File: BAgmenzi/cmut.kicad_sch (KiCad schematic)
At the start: 14 parts, among them J4 connector for CMUT

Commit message: added libraries, other changes in sch, started pcb
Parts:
- renumbered C60 to C61, C61 to C62, C62 to C63, R45 to R41, R44 to R43, R43 to R44
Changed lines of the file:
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@@
 		(dnp no)
 		(fields_autoplaced yes)
-		(property "Reference" "R45"
+		(property "Reference" "R41"
 			(at 134.62 41.9099 0)
 			(effects
@@
 			(project "BAgmenzi"
 				(path "/8cc4acae-3f14-463c-b0a0-3bc1c8d05954/edb8e8bc-fb53-4a31-8600-d64a48325b03"
-					(reference "R45")
+					(reference "R41")
 					(unit 1)
 				)
@@
 		(dnp no)
 		(fields_autoplaced yes)
-		(property "Reference" "C62"
+		(property "Reference" "C63"
 			(at 142.24 130.8099 0)
 			(effects
@@
 			(project ""
 				(path "/8cc4acae-3f14-463c-b0a0-3bc1c8d05954/edb8e8bc-fb53-4a31-8600-d64a48325b03"
-					(reference "C62")
+					(reference "C63")
 					(unit 1)
 				)
@@
 		(on_board yes)
 		(dnp no)
-		(property "Reference" "C61"
+		(property "Reference" "C62"
 			(at 118.11 130.302 0)
 			(effects
@@
 			(project "BAgmenzi"
 				(path "/8cc4acae-3f14-463c-b0a0-3bc1c8d05954/edb8e8bc-fb53-4a31-8600-d64a48325b03"
-					(reference "C61")
+					(reference "C62")
 					(unit 1)
 				)
@@
 		(dnp no)
 		(fields_autoplaced yes)
-		(property "Reference" "R44"
+		(property "Reference" "R43"
 			(at 127 69.8499 0)
 			(effects
@@
 			(project "BAgmenzi"
 				(path "/8cc4acae-3f14-463c-b0a0-3bc1c8d05954/edb8e8bc-fb53-4a31-8600-d64a48325b03"
-					(reference "R44")
+					(reference "R43")
 					(unit 1)
 				)
@@
 		(on_board yes)
 		(dnp no)
-		(property "Reference" "C60"
+		(property "Reference" "C61"
 			(at 134.112 61.722 90)
 			(effects
@@
 			(project "BAgmenzi"
 				(path "/8cc4acae-3f14-463c-b0a0-3bc1c8d05954/edb8e8bc-fb53-4a31-8600-d64a48325b03"
-					(reference "C60")
+					(reference "C61")
 					(unit 1)
 				)
@@
 		(dnp no)
 		(fields_autoplaced yes)
-		(property "Reference" "R43"
+		(property "Reference" "R44"
 			(at 123.19 113.03 90)
 			(effects
@@
 			(project "BAgmenzi"
 				(path "/8cc4acae-3f14-463c-b0a0-3bc1c8d05954/edb8e8bc-fb53-4a31-8600-d64a48325b03"
-					(reference "R43")
-					(unit 1)
-				)
+					(reference "R44")
+					(unit 1)
+				)

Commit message: changed VRX rail and deleted U12
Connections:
- net PULSE_HV_IN renamed PULSE_HV
- net RX_OUT renamed RX_IN
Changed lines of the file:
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@@
 		)
 	)
-	(hierarchical_label "PULSE_HV_IN"
+	(global_label "PULSE_HV"
 		(shape input)
 		(at 68.58 87.63 180)
+		(fields_autoplaced yes)
 		(effects
 			(font
@@
 			(justify right)
 		)
+		(property "Intersheetrefs" "${INTERSHEET_REFS}"
+			(at 56.221 87.63 0)
+			(effects
+				(font
+					(size 1.27 1.27)
+				)
+				(justify right)
+			)
+		)
 	)
-	(hierarchical_label "RX_OUT"
+	(global_label "RX_IN"
 		(shape output)
 		(at 67.31 93.98 180)
+		(fields_autoplaced yes)
 		(effects
 			(font
@@
 			(justify right)
 		)
+		(property "Intersheetrefs" "${INTERSHEET_REFS}"
+			(at 58.9424 93.98 0)
+			(effects
+				(font
+					(size 1.27 1.27)
+				)
+				(justify right)
+			)
+		)
 	)

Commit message: started layout, front v backside
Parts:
- C61, C62, C63, R43, R44: footprint (none) -> EEG_PcbLib:0402
- J4: footprint (none) -> cmut_dummy:cmut-dummy
- JP1, JP2, JP3, JP4, JP5: footprint (none) -> Jumper:SolderJumper-3_P1.3mm_Open_Pad1.0x1.5mm
- R41, R42: footprint (none) -> Resistor_SMD:R_0402_1005Metric
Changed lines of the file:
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@@
 			)
 		)
-		(property "Footprint" ""
+		(property "Footprint" "Resistor_SMD:R_0402_1005Metric"
 			(at 130.302 43.18 90)
 			(effects
@@
 			)
 		)
-		(property "Footprint" ""
+		(property "Footprint" "EEG_PcbLib:0402"
 			(at 139.3952 135.89 0)
 			(effects
@@
 			)
 		)
-		(property "Footprint" ""
+		(property "Footprint" "cmut_dummy:cmut-dummy"
 			(at 152.4 90.17 0)
 			(effects
@@
 		(instances
 			(project ""
+				(path "/8cc4acae-3f14-463c-b0a0-3bc1c8d05954/d463870e-9fcf-4af5-ace7-dfb7bf5f63b9"
+					(reference "J4")
+					(unit 1)
+				)
 				(path "/8cc4acae-3f14-463c-b0a0-3bc1c8d05954/edb8e8bc-fb53-4a31-8600-d64a48325b03"
 					(reference "J4")
@@
 			)
 		)
-		(property "Footprint" ""
+		(property "Footprint" "EEG_PcbLib:0402"
 			(at 131.7752 135.89 0)
 			(effects
@@
 			)
 		)
-		(property "Footprint" ""
+		(property "Footprint" "EEG_PcbLib:0402"
 			(at 122.682 71.12 90)
 			(effects
@@
 			)
 		)
-		(property "Footprint" ""
+		(property "Footprint" "Jumper:SolderJumper-3_P1.3mm_Open_Pad1.0x1.5mm"
 			(at 124.46 53.34 0)
 			(effects
@@
 			)
 		)
-		(property "Footprint" ""
+		(property "Footprint" "Jumper:SolderJumper-3_P1.3mm_Open_Pad1.0x1.5mm"
 			(at 144.78 113.03 0)
 			(effects
@@
 			)
 		)
-		(property "Footprint" ""
+		(property "Footprint" "Resistor_SMD:R_0402_1005Metric"
 			(at 87.122 71.12 90)
 			(effects
@@
 			)
 		)
-		(property "Footprint" ""
+		(property "Footprint" "EEG_PcbLib:0402"
 			(at 127 64.4652 0)
 			(effects
@@
 			)
 		)
-		(property "Footprint" ""
+		(property "Footprint" "Jumper:SolderJumper-3_P1.3mm_Open_Pad1.0x1.5mm"
 			(at 128.27 35.56 0)
 			(effects
@@
 			)
 		)
-		(property "Footprint" ""
+		(property "Footprint" "Jumper:SolderJumper-3_P1.3mm_Open_Pad1.0x1.5mm"
 			(at 88.9 48.26 0)
 			(effects
@@
 			)
 		)
-		(property "Footprint" ""
+		(property "Footprint" "Jumper:SolderJumper-3_P1.3mm_Open_Pad1.0x1.5mm"
 			(at 95.25 35.56 0)
 			(effects
@@
 			)
 		)
-		(property "Footprint" ""
+		(property "Footprint" "EEG_PcbLib:0402"
 			(at 123.19 121.158 90)
 			(effects

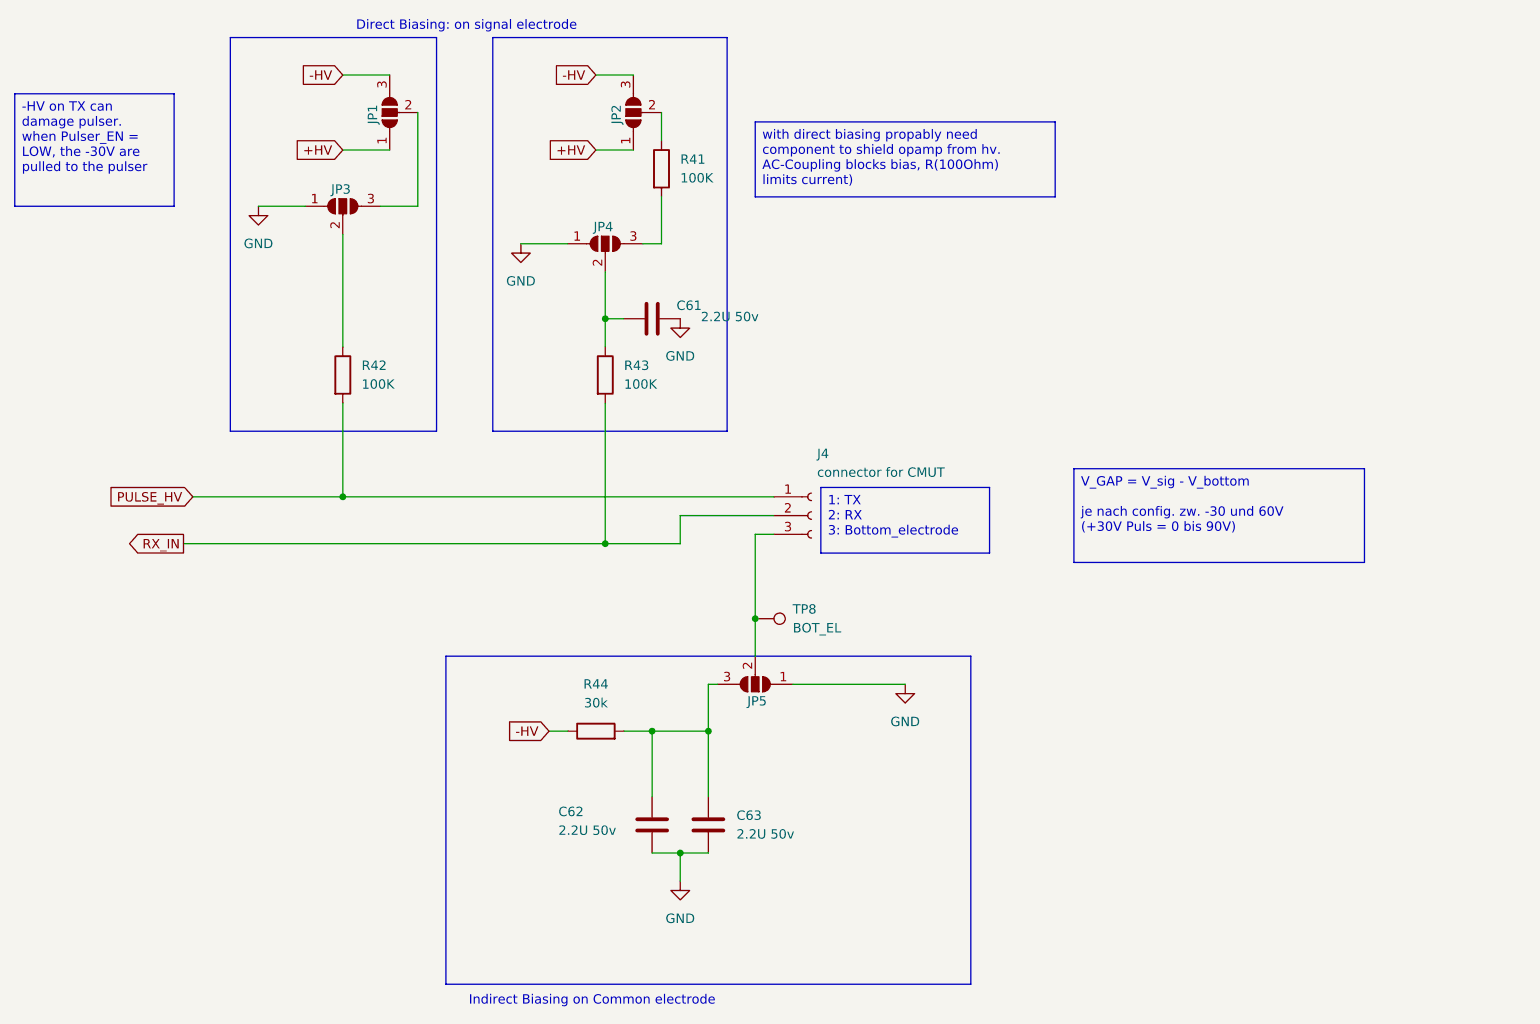
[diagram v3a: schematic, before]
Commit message: added polyCMUT footprint, changed enables, more compact
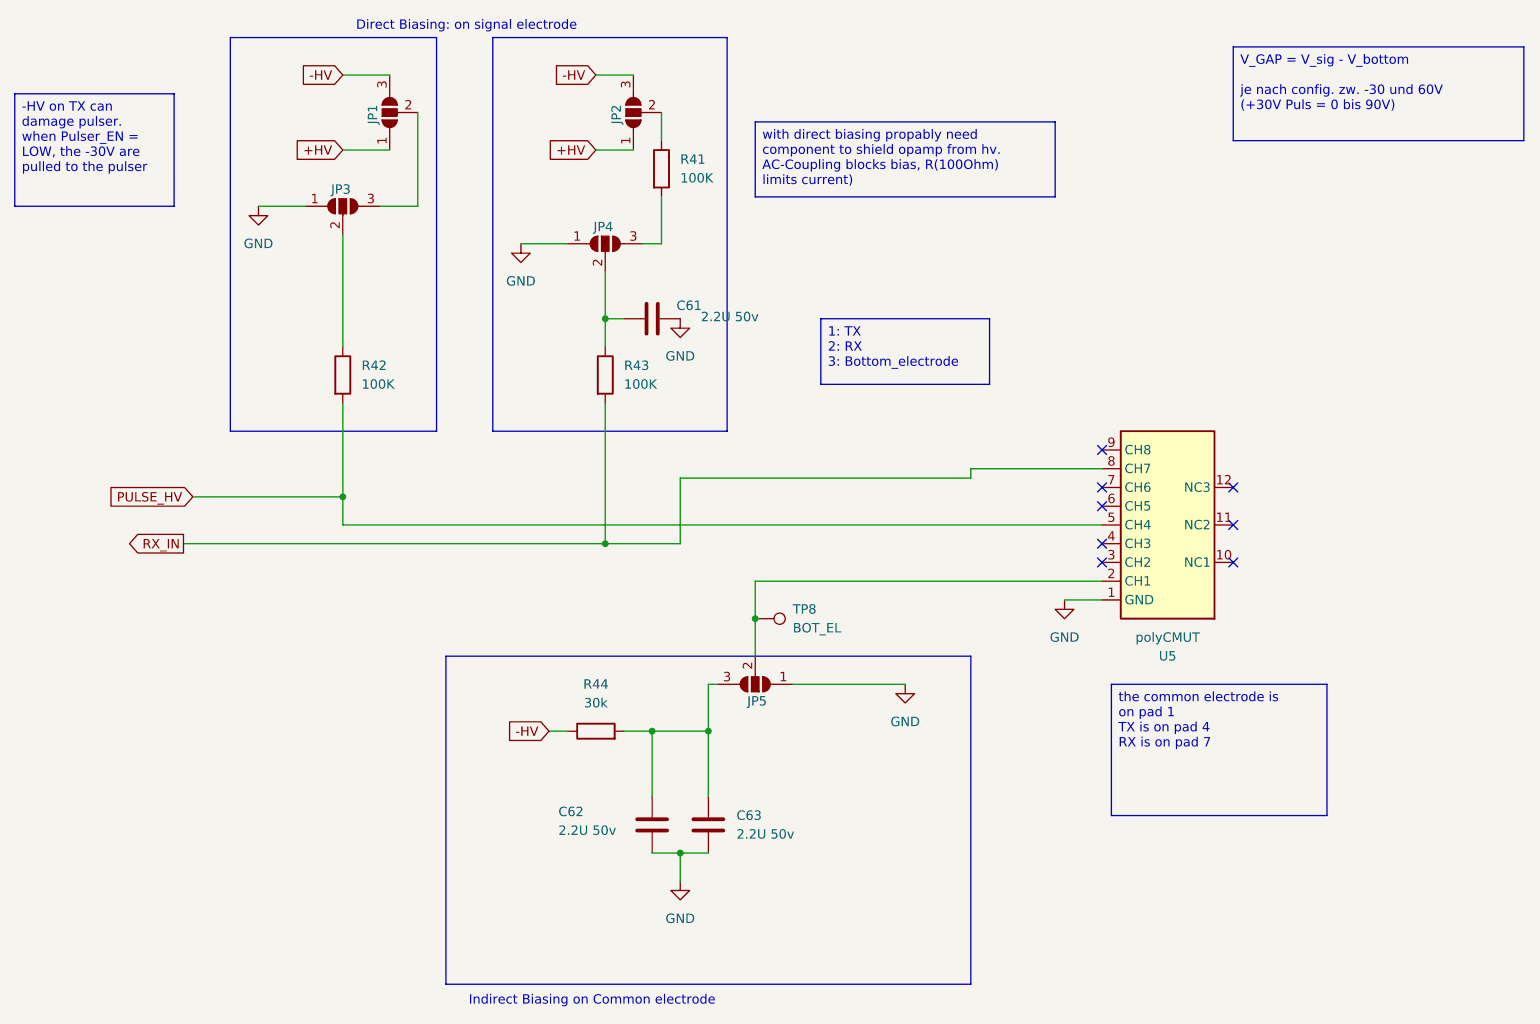
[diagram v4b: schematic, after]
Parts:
- removed J4: connector for CMUT, cmut_dummy:cmut-dummy, symbol Connector:Conn_01x03_Socket
- added U5: polyCMUT, polyCMUT:polyCMUT, symbol polyCMUT:polyCMUT
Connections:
- net GND: now also U5.1 (GND)
- net PULSE_HV: now also U5.5 (CH4)
- net RX_IN: now also U5.8 (CH7)
- net at JP5.2 (C), TP8.1: now also U5.2 (CH1)
- no-connect marks 0 -> 8
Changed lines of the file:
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@@
 	(text_box "V_GAP = V_sig - V_bottom\n\nje nach config. zw. -30 und 60V (+30V Puls = 0 bis 90V)\n"
 		(exclude_from_sim no)
-		(at 187.96 83.82 0)
+		(at 209.55 26.67 0)
 		(size 39.37 12.7)
 		(margins 0.9525 0.9525 0.9525 0.9525)
@@
 		)
 	)
+	(text_box "the common electrode is on pad 1\nTX is on pad 4\nRX is on pad 7"
+		(exclude_from_sim no)
+		(at 193.04 113.03 0)
+		(size 29.21 17.78)
+		(margins 0.9525 0.9525 0.9525 0.9525)
+		(stroke
+			(width 0)
+			(type solid)
+		)
+		(fill
+			(type none)
+		)
+		(effects
+			(font
+				(size 1.27 1.27)
+			)
+			(justify left top)
+		)
+	)
 	(text_box "1: TX\n2: RX\n3: Bottom_electrode\n"
 		(exclude_from_sim no)
-		(at 153.67 86.36 0)
+		(at 153.67 63.5 0)
 		(size 22.86 8.89)
 		(margins 0.9525 0.9525 0.9525 0.9525)
@@
 		(color 0 0 0 0)
 	)
+	(no_connect
+		(at 209.55 91.44)
+	)
+	(no_connect
+		(at 209.55 86.36)
+	)
+	(no_connect
+		(at 191.77 86.36)
+	)
+	(no_connect
+		(at 191.77 81.28)
+	)
+	(no_connect
+		(at 209.55 96.52)
+	)
+	(no_connect
+		(at 191.77 93.98)
+	)
+	(no_connect
+		(at 191.77 96.52)
+	)
+	(no_connect
+		(at 191.77 88.9)
+	)
 	(wire
 		(pts
@@
 	(wire
 		(pts
+			(xy 173.99 85.09) (xy 173.99 83.82)
+		)
+		(stroke
+			(width 0)
+			(type default)
+		)
+	)
+	(wire
+		(pts
 			(xy 127 119.38) (xy 130.81 119.38)
 		)
@@
 	(wire
 		(pts
-			(xy 88.9 87.63) (xy 147.32 87.63)
+			(xy 88.9 91.44) (xy 191.77 91.44)
 		)
 		(stroke
@@
 	(wire
 		(pts
-			(xy 147.32 92.71) (xy 144.78 92.71)
-		)
-		(stroke
-			(width 0)
-			(type default)
-		)
-	)
-	(wire
-		(pts
 			(xy 88.9 74.93) (xy 88.9 87.63)
 		)
@@
 	(wire
 		(pts
-			(xy 147.32 90.17) (xy 134.62 90.17)
+			(xy 134.62 85.09) (xy 173.99 85.09)
 		)
 		(stroke
@@
 	(wire
 		(pts
+			(xy 88.9 91.44) (xy 88.9 87.63)
+		)
+		(stroke
+			(width 0)
+			(type default)
+		)
+	)
+	(wire
+		(pts
 			(xy 123.19 30.48) (xy 128.27 30.48)
 		)
@@
 	(wire
 		(pts
+			(xy 173.99 83.82) (xy 191.77 83.82)
+		)
+		(stroke
+			(width 0)
+			(type default)
+		)
+	)
+	(wire
+		(pts
 			(xy 132.08 46.99) (xy 132.08 53.34)
 		)
@@
 	(wire
 		(pts
-			(xy 134.62 90.17) (xy 134.62 93.98)
+			(xy 134.62 85.09) (xy 134.62 93.98)
+		)
+		(stroke
+			(width 0)
+			(type default)
+		)
+	)
+	(wire
+		(pts
+			(xy 144.78 99.06) (xy 191.77 99.06)
 		)
 		(stroke
@@
 	(wire
 		(pts
-			(xy 144.78 92.71) (xy 144.78 104.14)
+			(xy 144.78 99.06) (xy 144.78 104.14)
+		)
+		(stroke
+			(width 0)
+			(type default)
+		)
+	)
+	(wire
+		(pts
+			(xy 186.69 101.6) (xy 191.77 101.6)
 		)
 		(stroke
@@
 	)
 	(symbol
-		(lib_id "Connector:Conn_01x03_Socket")
-		(at 152.4 90.17 0)
-		(unit 1)
-		(exclude_from_sim no)
-		(in_bom yes)
-		(on_board yes)
-		(dnp no)
-		(property "Reference" "J4"
-			(at 153.162 81.788 0)
-			(effects
-				(font
-					(size 1.27 1.27)
-				)
-				(justify left)
-			)
-		)
-		(property "Value" "connector for CMUT"
-			(at 153.162 84.328 0)
-			(effects
-				(font
-					(size 1.27 1.27)
-				)
-				(justify left)
-			)
-		)
-		(property "Footprint" "cmut_dummy:cmut-dummy"
-			(at 152.4 90.17 0)
-			(effects
-				(font
-					(size 1.27 1.27)
-				)
-				(hide yes)
-			)
-		)
-		(property "Datasheet" "~"
-			(at 152.4 90.17 0)
-			(effects
-				(font
-					(size 1.27 1.27)
-				)
-				(hide yes)
-			)
-		)
-		(property "Description" "Generic connector, single row, 01x03, script generated"
-			(at 152.4 90.17 0)
-			(effects
-				(font
-					(size 1.27 1.27)
-				)
-				(hide yes)
-			)
-		)
-		(pin "1"
-		)
-		(pin "2"
-		)
-		(pin "3"
-		)
-		(instances
-			(project ""
-				(path "/8cc4acae-3f14-463c-b0a0-3bc1c8d05954/d463870e-9fcf-4af5-ace7-dfb7bf5f63b9"
-					(reference "J4")
-					(unit 1)
-				)
-				(path "/8cc4acae-3f14-463c-b0a0-3bc1c8d05954/edb8e8bc-fb53-4a31-8600-d64a48325b03"
-					(reference "J4")
-					(unit 1)
-				)
-			)
-		)
-	)
-	(symbol
 		(lib_id "Device:C")
 		(at 130.81 132.08 0)
@@
 	)
 	(symbol
+		(lib_id "polyCMUT:polyCMUT")
+		(at 201.93 91.44 180)
+		(unit 1)
+		(exclude_from_sim no)
+		(in_bom yes)
+		(on_board yes)
+		(dnp no)
+		(fields_autoplaced yes)
+		(property "Reference" "U5"
+			(at 200.66 109.22 0)
+			(effects
+				(font
+					(size 1.27 1.27)
+				)
+			)
+		)
+		(property "Value" "polyCMUT"
+			(at 200.66 106.68 0)
+			(effects
+				(font
+					(size 1.27 1.27)
+				)
+			)
+		)
+		(property "Footprint" "polyCMUT:polyCMUT"
+			(at 201.93 91.44 0)
+			(effects
+				(font
+					(size 1.27 1.27)
+				)
+				(hide yes)
+			)
+		)
+		(property "Datasheet" ""
+			(at 201.93 91.44 0)
+			(effects
+				(font
+					(size 1.27 1.27)
+				)
+				(hide yes)
+			)
+		)
+		(property "Description" "polyCMUT module, 16.0 x 16.0 x 0.8 mm. Right-edge castellations are GND and CH1-CH8. Left-edge castellations NC1-NC3 are plated but have no net on the module."
+			(at 201.93 91.44 0)
+			(effects
+				(font
+					(size 1.27 1.27)
+				)
+				(hide yes)
+			)
+		)
+		(pin "5"
+		)
+		(pin "2"
+		)
+		(pin "4"
+		)
+		(pin "1"
+		)
+		(pin "11"
+		)
+		(pin "12"
+		)
+		(pin "10"
+		)
+		(pin "3"
+		)
+		(pin "9"
+		)
+		(pin "8"
+		)
+		(pin "6"
+		)
+		(pin "7"
+		)
+		(instances
+			(project ""
+				(path "/8cc4acae-3f14-463c-b0a0-3bc1c8d05954/edb8e8bc-fb53-4a31-8600-d64a48325b03"
+					(reference "U5")
+					(unit 1)
+				)
+			)
+		)
+	)
+	(symbol
 		(lib_id "Device:C")
 		(at 130.81 63.5 270)
@@
 					(unit 1)
 				)
+			)
+		)
+	)
+	(symbol
+		(lib_id "power:GND")
+		(at 186.69 101.6 0)
+		(unit 1)
+		(exclude_from_sim no)
+		(in_bom yes)
+		(on_board yes)
+		(dnp no)
+		(fields_autoplaced yes)
+		(property "Reference" "#PWR091"
+			(at 186.69 107.95 0)
+			(effects
+				(font
+					(size 1.27 1.27)
+				)
+				(hide yes)
+			)
+		)
+		(property "Value" "GND"
+			(at 186.69 106.68 0)
+			(effects
+				(font
+					(size 1.27 1.27)
+				)
+			)
+		)
+		(property "Footprint" ""
+			(at 186.69 101.6 0)
+			(effects
+				(font
+					(size 1.27 1.27)
+				)
+				(hide yes)
+			)
+		)
+		(property "Datasheet" ""
+			(at 186.69 101.6 0)
+			(effects
+				(font
+					(size 1.27 1.27)
+				)
+				(hide yes)
+			)
+		)
+		(property "Description" "Power symbol creates a global label with name \"GND\" , ground"
+			(at 186.69 101.6 0)
+			(effects
+				(font
+					(size 1.27 1.27)
+				)
+				(hide yes)
+			)
+		)
+		(pin "1"
+		)
+		(instances
+			(project ""
+				(path "/8cc4acae-3f14-463c-b0a0-3bc1c8d05954/edb8e8bc-fb53-4a31-8600-d64a48325b03"
+					(reference "#PWR091")
+					(unit 1)
+				)

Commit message: part numbers added
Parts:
- C61, C62, C63: value 2.2U 50v -> 2.2u 50V; footprint EEG_PcbLib:0402 -> Capacitor_SMD:C_0603_1608Metric
- R41, R42, R43: value 100K -> 100k; LCSC Part # (none) -> C22369186
- R44: LCSC Part # (none) -> C2909347
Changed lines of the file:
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@@
 			)
 		)
-		(property "Value" "100K"
+		(property "Value" "100k"
 			(at 134.62 44.4499 0)
 			(effects
@@
 		)
 		(property "Description" "Resistor"
+			(at 132.08 43.18 0)
+			(effects
+				(font
+					(size 1.27 1.27)
+				)
+				(hide yes)
+			)
+		)
+		(property "LCSC Part #" "C22369186"
 			(at 132.08 43.18 0)
 			(effects
@@
 			)
 		)
-		(property "Value" "2.2U 50v"
+		(property "Value" "2.2u 50V"
 			(at 142.24 133.3499 0)
 			(effects
@@
 			)
 		)
-		(property "Footprint" "EEG_PcbLib:0402"
+		(property "Footprint" "Capacitor_SMD:C_0603_1608Metric"
 			(at 139.3952 135.89 0)
 			(effects
@@
 			)
 		)
-		(property "Value" "2.2U 50v"
+		(property "Value" "2.2u 50V"
 			(at 118.11 132.842 0)
 			(effects
@@
 			)
 		)
-		(property "Footprint" "EEG_PcbLib:0402"
+		(property "Footprint" "Capacitor_SMD:C_0603_1608Metric"
 			(at 131.7752 135.89 0)
 			(effects
@@
 			)
 		)
-		(property "Value" "100K"
+		(property "Value" "100k"
 			(at 127 72.3899 0)
 			(effects
@@
 		)
 		(property "Description" "Resistor"
+			(at 124.46 71.12 0)
+			(effects
+				(font
+					(size 1.27 1.27)
+				)
+				(hide yes)
+			)
+		)
+		(property "LCSC Part #" "C22369186"
 			(at 124.46 71.12 0)
 			(effects
@@
 			)
 		)
-		(property "Value" "100K"
+		(property "Value" "100k"
 			(at 91.44 72.3899 0)
 			(effects
@@
 		)
 		(property "Description" "Resistor"
+			(at 88.9 71.12 0)
+			(effects
+				(font
+					(size 1.27 1.27)
+				)
+				(hide yes)
+			)
+		)
+		(property "LCSC Part #" "C22369186"
 			(at 88.9 71.12 0)
 			(effects
@@
 			)
 		)
-		(property "Value" "2.2U 50v"
+		(property "Value" "2.2u 50V"
 			(at 137.414 63.246 90)
 			(effects
@@
 			)
 		)
-		(property "Footprint" "EEG_PcbLib:0402"
+		(property "Footprint" "Capacitor_SMD:C_0603_1608Metric"
 			(at 127 64.4652 0)
 			(effects
@@
 			(effects
 				(font
+					(size 1.27 1.27)
+				)
+				(hide yes)
+			)
+		)
+		(property "LCSC Part #" "C2909347"
+			(at 123.19 119.38 90)
+			(effects
+				(font

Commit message: LCSC parts complete, changed L5andL6 footprint
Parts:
- C61, C62, C63: LCSC Part # (none) -> C668357
- R41, R42, R43: LCSC Part # C22369186 -> C192169
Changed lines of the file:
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@@
 			)
 		)
-		(property "LCSC Part #" "C22369186"
+		(property "LCSC Part #" "C192169 "
 			(at 132.08 43.18 0)
 			(effects
@@
 			)
 		)
+		(property "LCSC Part #" "C668357 "
+			(at 138.43 132.08 0)
+			(effects
+				(font
+					(size 1.27 1.27)
+				)
+				(hide yes)
+			)
+		)
 		(pin "2"
 		)
@@
 		)
 		(property "Description" "Unpolarized capacitor"
+			(at 130.81 132.08 0)
+			(effects
+				(font
+					(size 1.27 1.27)
+				)
+				(hide yes)
+			)
+		)
+		(property "LCSC Part #" "C668357 "
 			(at 130.81 132.08 0)
 			(effects
@@
 			)
 		)
-		(property "LCSC Part #" "C22369186"
+		(property "LCSC Part #" "C192169 "
 			(at 124.46 71.12 0)
 			(effects
@@
 			)
 		)
-		(property "LCSC Part #" "C22369186"
+		(property "LCSC Part #" "C192169 "
 			(at 88.9 71.12 0)
 			(effects
@@
 			(effects
 				(font
+					(size 1.27 1.27)
+				)
+				(hide yes)
+			)
+		)
+		(property "LCSC Part #" "C668357 "
+			(at 130.81 63.5 90)
+			(effects
+				(font

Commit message: corrected LCSC numbers, other changes, Testpoints
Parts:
- C61, C62, C63: LCSC Part # C668357 -> C668357
- R41, R42, R43: LCSC Part # C192169 -> C192169
- TP8: footprint (none) -> TestPoint:TestPoint_Pad_D1.0mm
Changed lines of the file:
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@@
 			)
 		)
-		(property "LCSC Part #" "C192169 "
+		(property "LCSC Part #" "C192169"
 			(at 132.08 43.18 0)
 			(effects
@@
 			)
 		)
-		(property "LCSC Part #" "C668357 "
+		(property "LCSC Part #" "C668357"
 			(at 138.43 132.08 0)
 			(effects
@@
 			)
 		)
-		(property "LCSC Part #" "C668357 "
+		(property "LCSC Part #" "C668357"
 			(at 130.81 132.08 0)
 			(effects
@@
 			)
 		)
-		(property "LCSC Part #" "C192169 "
+		(property "LCSC Part #" "C192169"
 			(at 124.46 71.12 0)
 			(effects
@@
 			)
 		)
-		(property "LCSC Part #" "C192169 "
+		(property "LCSC Part #" "C192169"
 			(at 88.9 71.12 0)
 			(effects
@@
 			)
 		)
-		(property "LCSC Part #" "C668357 "
+		(property "LCSC Part #" "C668357"
 			(at 130.81 63.5 90)
 			(effects
@@
 			)
 		)
-		(property "Footprint" ""
+		(property "Footprint" "TestPoint:TestPoint_Pad_D1.0mm"
 			(at 144.78 109.22 0)
 			(effects
